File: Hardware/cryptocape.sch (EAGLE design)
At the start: 46 parts, among them J1 AVR_SPI_PRG_6PTH, U2 ATMEGA328P, U3 EEPROM-I2CSMD, Y1 16MHz

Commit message: Adds ATAES123 and Cryptotronix Logo
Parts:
- added AES1: ATAES132, cryptotronix:ATAES132
- added C4: 0.1uF, SparkFun-Capacitors:0.1UF-25V(+80/-20%)(0603)
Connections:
- new net AUTH0: AES1.AUTHO, U$2P8.GPIO_45
- net 3.3V: now also AES1.VCC, C4.1
- net GND: now also AES1.GND, C4.2
- net I2C2_SCL: now also AES1.SCL
- net I2C2_SDA: now also AES1.SDA
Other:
- note added: "AES-128 (ATAES132)"
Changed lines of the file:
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@@
 <part name="JP13" library="SparkFun-Passives" deviceset="JUMPER-2" device="PTH" value="Jump for Read/Write"/>
 <part name="JP14" library="SparkFun-Passives" deviceset="JUMPER-2" device="PTH"/>
+<part name="AES1" library="cryptotronix" deviceset="ATAES132" device=""/>
+<part name="GND11" library="SparkFun-Aesthetics" deviceset="GND" device=""/>
+<part name="SUPPLY23" library="SparkFun-Aesthetics" deviceset="3.3V" device=""/>
+<part name="C4" library="SparkFun-Capacitors" deviceset="0.1UF-25V(+80/-20%)(0603)" device="" value="0.1uF"/>
+<part name="GND28" library="SparkFun-Aesthetics" deviceset="GND" device=""/>
+<part name="SUPPLY24" library="SparkFun-Aesthetics" deviceset="3.3V" device=""/>
 </parts>
 <sheets>
@@
 ATSHA204 0x64
 RTC      0x68</text>
+<text x="365.76" y="36.068" size="2.54" layer="94" font="vector">AES-128 (ATAES132)</text>
 </plain>
 <instances>
@@
 </instance>
 <instance part="JP14" gate="A" x="121.92" y="38.1" rot="R270"/>
+<instance part="AES1" gate="G$1" x="381" y="50.8"/>
+<instance part="GND11" gate="1" x="358.14" y="38.1"/>
+<instance part="SUPPLY23" gate="G$1" x="403.86" y="53.34"/>
+<instance part="C4" gate="G$1" x="421.64" y="45.72"/>
+<instance part="GND28" gate="1" x="421.64" y="38.1"/>
+<instance part="SUPPLY24" gate="G$1" x="421.64" y="53.34"/>
 </instances>
 <busses>
@@
 <wire x1="147.32" y1="182.88" x2="147.32" y2="177.8" width="0.1524" layer="91"/>
 </segment>
+<segment>
+<pinref part="GND11" gate="1" pin="GND"/>
+<wire x1="358.14" y1="40.64" x2="358.14" y2="45.72" width="0.1524" layer="91"/>
+<pinref part="AES1" gate="G$1" pin="GND"/>
+<wire x1="358.14" y1="45.72" x2="368.3" y2="45.72" width="0.1524" layer="91"/>
+</segment>
+<segment>
+<pinref part="GND28" gate="1" pin="GND"/>
+<pinref part="C4" gate="G$1" pin="2"/>
+<wire x1="421.64" y1="40.64" x2="421.64" y2="43.18" width="0.1524" layer="91"/>
+</segment>
 </net>
 <net name="VBAT" class="0">
@@
 <label x="170.18" y="162.56" size="1.27" layer="95" xref="yes"/>
 </segment>
+<segment>
+<pinref part="AES1" gate="G$1" pin="SCL"/>
+<wire x1="393.7" y1="48.26" x2="403.86" y2="48.26" width="0.1524" layer="91"/>
+<label x="403.86" y="48.26" size="1.27" layer="95" xref="yes"/>
+</segment>
 </net>
 <net name="I2C2_SDA" class="0">
@@
 <wire x1="165.1" y1="160.02" x2="170.18" y2="160.02" width="0.1524" layer="91"/>
 <label x="170.18" y="160.02" size="1.27" layer="95" xref="yes"/>
+</segment>
+<segment>
+<pinref part="AES1" gate="G$1" pin="SDA"/>
+<wire x1="393.7" y1="45.72" x2="403.86" y2="45.72" width="0.1524" layer="91"/>
+<label x="403.86" y="45.72" size="1.27" layer="95" xref="yes"/>
 </segment>
 </net>
@@
 <wire x1="177.8" y1="175.26" x2="177.8" y2="182.88" width="0.1524" layer="91"/>
 </segment>
+<segment>
+<pinref part="SUPPLY23" gate="G$1" pin="3.3V"/>
+<pinref part="AES1" gate="G$1" pin="VCC"/>
+<wire x1="403.86" y1="53.34" x2="393.7" y2="53.34" width="0.1524" layer="91"/>
+</segment>
+<segment>
+<pinref part="C4" gate="G$1" pin="1"/>
+<pinref part="SUPPLY24" gate="G$1" pin="3.3V"/>
+<wire x1="421.64" y1="50.8" x2="421.64" y2="53.34" width="0.1524" layer="91"/>
+</segment>
 </net>
 <net name="N$18" class="0">
@@
 </segment>
 </net>
+<net name="AUTH0" class="0">
+<segment>
+<pinref part="AES1" gate="G$1" pin="AUTHO"/>
+<wire x1="368.3" y1="50.8" x2="358.14" y2="50.8" width="0.1524" layer="91"/>
+<label x="358.14" y="50.8" size="1.778" layer="95" rot="R180" xref="yes"/>
+</segment>
+<segment>
+<pinref part="U$2" gate="P8" pin="GPIO_45"/>
+<wire x1="50.8" y1="251.46" x2="40.64" y2="251.46" width="0.1524" layer="91"/>
+<label x="40.64" y="251.46" size="1.778" layer="95" rot="R180" xref="yes"/>
+</segment>
+</net>

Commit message: finished layout with lables.  Board is in state for review
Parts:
- removed JP10, JP11, JP12, JP9: M161X16_NO_SILK, SparkFun-Connectors:M161X16_NO_SILK
- removed U$1: DS1077, SparkFun-FreqCtrl:DS1077
- removed Y1: 16MHz, SparkFun-FreqCtrl:RESONATOR16MHZ
- added C5: .1uf, SparkFun-Capacitors:0.1UF-25V(+80/-20%)(0603)
- added D1: GREEN, SparkFun-LED:LED-GREEN0603
- added R1: 10k, SparkFun-Resistors:10KOHM1/10W1%(0603)0603
- added R2: 1k, SparkFun-Resistors:1K-1%
- added U1: 33mhz, cryptotronix:OSCILLATOR
- added Y2: 8MHZ, SparkFun-FreqCtrl:RESONATOR8MHZ
- C10: value 10nF -> 0.1uF; device SparkFun-Capacitors:10NF/10000PF-50V-10%(0603) -> SparkFun-Capacitors:0.1UF-25V(+80/-20%)(0603)
- JP5: value M161X16_NO_SILK -> M11PTH; device SparkFun-Connectors:M161X16_NO_SILK -> SparkFun-Connectors:M11PTH
- JP6: value M161X16_NO_SILK -> (none); device SparkFun-Connectors:M161X16_NO_SILK -> SparkFun-Connectors:M04PTH
- JP7, JP8: value M161X16_NO_SILK -> M02PTH; device SparkFun-Connectors:M161X16_NO_SILK -> SparkFun-Connectors:M02PTH
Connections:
- removed net PC0: JP5.6, U2.PC0(ADC0)
- removed net PC1: JP5.7, U2.PC1(ADC1)
- removed net PC2: JP5.8, U2.PC2(ADC2)
- removed net PD2: JP5.11, U2.PD2(INT0)
- removed net PD3: JP5.12, U2.PD3(INT1)
- removed net PD4: JP5.13, U2.PD4(XCK/T0)
- removed net PD5: JP5.14, U2.PD5(T1)
- new net A0: JP6.4, U2.PC0(ADC0)
- new net A1: JP6.3, U2.PC1(ADC1)
- new net A2: JP6.2, U2.PC2(ADC2)
- new net A3: JP6.1, U2.PC3(ADC3)
- new net D10: JP5.11, U2.PB2(SS/OC1B)
- new net D2: JP5.3, U2.PD2(INT0)
- new net D3: JP5.4, U2.PD3(INT1)
- new net D4: JP5.5, U2.PD4(XCK/T0)
- new net D5: JP5.6, U2.PD5(T1)
- new net D6: JP5.7, U2.PD6(AIN0)
- new net D7: JP5.8, U2.PD7(AIN1)
- new net D8: JP5.9, U2.PB0(ICP)
- new net D9: JP5.10, U2.PB1(OC1A)
- new net N$12: D1.A, R2.1
- net 3.3V: now also C5.1, JP5.2, R1.2, U1.VCC; no longer JP5.15, U$1.VCC
- net AT328P_RST: now also R1.1
- net D0: now also JP8.1
- net D0': no longer JP5.5
- net D1: now also JP8.2
- net D1': no longer JP5.4
- net GND: now also C5.2, D1.C, JP5.1, U1.GND, Y2.2; no longer JP5.16, U$1.GND, Y1.2
- net I2C2_SCL: now also JP7.1; no longer JP5.10
- net I2C2_SDA: now also JP7.2; no longer JP5.9
- net N$4: now also Y2.1; no longer Y1.1
- net N$5: now also Y2.3; no longer Y1.3
- net SCK: now also R2.2
- net TPM_CLK: now also U1.OUT; no longer U$1.OUT1
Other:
- note removed: "Clock for TPM"
- moved on the sheet: C10, C11, C12, C13, C14, C2, C7, C8, R6, TPM1

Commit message: added authors on Schematic
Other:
- note added: "Josh Datko / Casey Kuhns"
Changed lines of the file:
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@@
 <sheet>
 <plain>
-<text x="358.14" y="7.62" size="3.81" layer="94" font="vector">Cryptotronix</text>
+<text x="350.52" y="7.62" size="2.54" layer="94">Cryptotronix</text>
 <wire x1="0" y1="116.84" x2="142.24" y2="116.84" width="0.1524" layer="94"/>
 <wire x1="142.24" y1="116.84" x2="142.24" y2="187.96" width="0.1524" layer="94"/>
@@
 RTC      0x68</text>
 <text x="365.76" y="36.068" size="2.54" layer="94" font="vector">AES-128 (ATAES132)</text>
+<text x="350.52" y="10.16" size="2.54" layer="94">Josh Datko / Casey Kuhns</text>
 </plain>
 <instances>

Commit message: added version on schematic
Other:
- note added: "v01"
- note removed: "A"
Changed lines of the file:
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@@
 <text x="200.66" y="121.92" size="2.54" layer="94" font="vector">Prototype Headers</text>
 <wire x1="287.02" y1="187.96" x2="287.02" y2="116.84" width="0.1524" layer="94"/>
-<text x="421.64" y="7.62" size="3.81" layer="94" font="vector">A</text>
 <wire x1="287.02" y1="116.84" x2="287.02" y2="60.96" width="0.1524" layer="94"/>
 <wire x1="231.14" y1="116.84" x2="287.02" y2="116.84" width="0.1524" layer="94"/>
@@
 <text x="365.76" y="36.068" size="2.54" layer="94" font="vector">AES-128 (ATAES132)</text>
 <text x="350.52" y="10.16" size="2.54" layer="94">Josh Datko / Casey Kuhns</text>
+<text x="421.64" y="7.62" size="2.54" layer="94">v01</text>
 </plain>
 <instances>

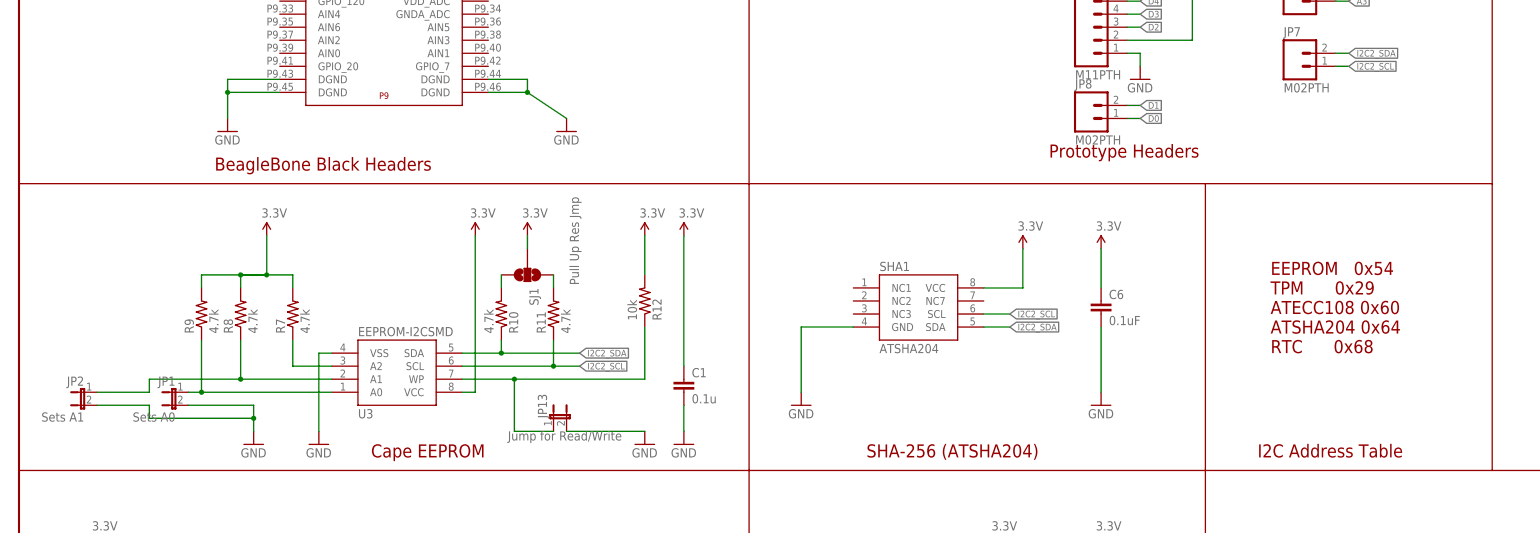
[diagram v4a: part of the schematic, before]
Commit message: Superficial changes to schematic and board.
- Fixes bent wire on schematic on BBB header.
- Changes "set" to "clear" on EEPROM
- Adds ATATES132 to I2C address list
- Resorts the list by address
- Changes "Atmel Trusted Platform Module" to TPM on brd
- Changes "MEGA328" to "m328P"
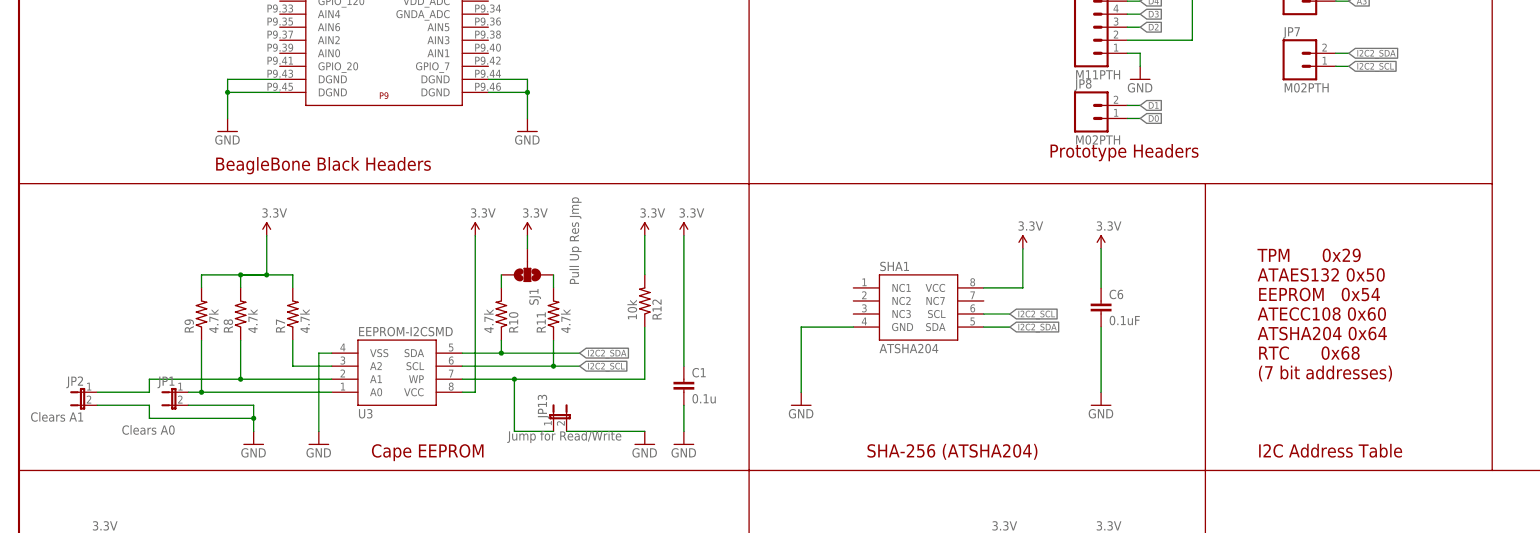
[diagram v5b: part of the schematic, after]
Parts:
- JP1: value Sets A0 -> Clears A0
- JP2: value Sets A1 -> Clears A1
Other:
- note added: "TPM 0x29 ATAES132 0x50 EEPROM 0x54 ATECC108 0x60 ATSHA204 0x64 RTC 0x68 (7 bit addresses)"
- note removed: "EEPROM 0x54 TPM 0x29 ATECC108 0x60 ATSHA204 0x64 RTC 0x68"
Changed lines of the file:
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@@
 <part name="R8" library="SparkFun-Resistors" deviceset="4.7KOHM1/10W1%(0603)" device="" value="4.7k"/>
 <part name="R9" library="SparkFun-Resistors" deviceset="4.7KOHM1/10W1%(0603)" device="" value="4.7k"/>
-<part name="JP2" library="SparkFun-Passives" deviceset="JUMPER-2" device="SMD-NO" value="Sets A1"/>
-<part name="JP1" library="SparkFun-Passives" deviceset="JUMPER-2" device="SMD-NO" value="Sets A0"/>
+<part name="JP2" library="SparkFun-Passives" deviceset="JUMPER-2" device="SMD-NO" value="Clears A1"/>
+<part name="JP1" library="SparkFun-Passives" deviceset="JUMPER-2" device="SMD-NO" value="Clears A0"/>
 <part name="GND10" library="SparkFun-Aesthetics" deviceset="GND" device=""/>
 <part name="C1" library="SparkFun-Capacitors" deviceset="0.1UF-25V(+80/-20%)(0603)" device="" value="0.1u"/>
@@
 <wire x1="231.14" y1="116.84" x2="287.02" y2="116.84" width="0.1524" layer="94"/>
 <text x="241.3" y="63.5" size="2.54" layer="94" font="vector">I2C Address Table</text>
-<text x="243.84" y="83.82" size="2.54" layer="94" font="vector">EEPROM   0x54
-TPM      0x29
+<text x="241.3" y="78.74" size="2.54" layer="94" font="vector">TPM      0x29
+ATAES132 0x50
+EEPROM   0x54
 ATECC108 0x60
 ATSHA204 0x64
-RTC      0x68</text>
+RTC      0x68
+(7 bit addresses)</text>
 <text x="365.76" y="36.068" size="2.54" layer="94" font="vector">AES-128 (ATAES132)</text>
 <text x="350.52" y="10.16" size="2.54" layer="94">Josh Datko / Casey Kuhns</text>
@@
 <instance part="R9" gate="G$1" x="35.56" y="91.44" rot="R90"/>
 <instance part="JP2" gate="A" x="12.7" y="76.2" rot="MR270"/>
-<instance part="JP1" gate="A" x="30.48" y="76.2" rot="MR270"/>
+<instance part="JP1" gate="A" x="30.48" y="76.2" smashed="yes" rot="MR270">
+<attribute name="NAME" x="30.48" y="77.47" size="1.778" layer="95" rot="MR0"/>
+<attribute name="VALUE" x="30.48" y="67.945" size="1.778" layer="96" rot="MR0"/>
+</instance>
 <instance part="GND10" gate="1" x="45.72" y="66.04"/>
 <instance part="C1" gate="G$1" x="129.54" y="76.2"/>
@@
 <instance part="GND23" gate="1" x="38.1" y="259.08"/>
 <instance part="GND24" gate="1" x="104.14" y="259.08"/>
-<instance part="GND25" gate="1" x="106.68" y="127"/>
+<instance part="GND25" gate="1" x="99.06" y="127"/>
 <instance part="GND26" gate="1" x="40.64" y="127"/>
 <instance part="J1" gate="G$1" x="281.94" y="33.02"/>
@@
 <wire x1="91.44" y1="134.62" x2="99.06" y2="134.62" width="0.1524" layer="91"/>
 <pinref part="GND25" gate="1" pin="GND"/>
-<wire x1="99.06" y1="134.62" x2="106.68" y2="129.54" width="0.1524" layer="91"/>
+<wire x1="99.06" y1="134.62" x2="99.06" y2="129.54" width="0.1524" layer="91"/>
 <pinref part="U$2" gate="P9" pin="DGND@4"/>
 <wire x1="91.44" y1="137.16" x2="99.06" y2="137.16" width="0.1524" layer="91"/>

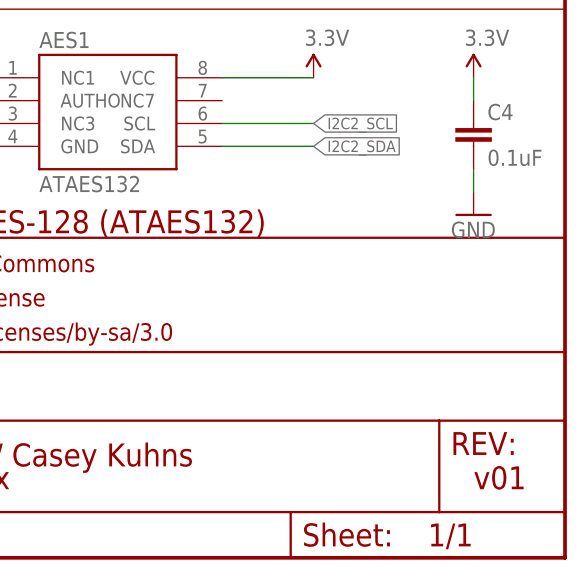
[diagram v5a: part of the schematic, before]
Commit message: added fiducials
regular local fiducials
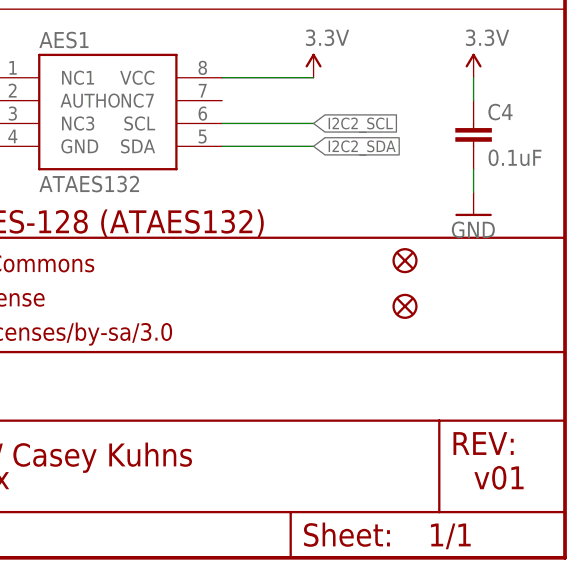
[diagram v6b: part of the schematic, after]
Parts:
- added FID1, FID2: FIDUCIAL1X2, SparkFun-Aesthetics:FIDUCIAL1X2
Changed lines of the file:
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@@
 <part name="JP7" library="SparkFun-Connectors" deviceset="M02" device="PTH"/>
 <part name="JP8" library="SparkFun-Connectors" deviceset="M02" device="PTH"/>
+<part name="FID1" library="SparkFun-Aesthetics" deviceset="FIDUCIAL" device="1X2"/>
+<part name="FID2" library="SparkFun-Aesthetics" deviceset="FIDUCIAL" device="1X2"/>
 </parts>
 <sheets>
@@
 <instance part="JP7" gate="G$1" x="248.92" y="139.7"/>
 <instance part="JP8" gate="G$1" x="208.28" y="129.54"/>
+<instance part="FID1" gate="G$1" x="414.02" y="33.02"/>
+<instance part="FID2" gate="G$1" x="414.02" y="27.94"/>
 </instances>
 <busses>
